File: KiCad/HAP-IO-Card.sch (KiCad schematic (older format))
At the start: 18 parts, among them U1 D1_Mini, U10 7400, U2 PCF8574, U3 PCF8574, U4 PCF8574, U5 PCF8574, U6 PCF8574, U7 PCF8574, U8 PCF8574, U9 PCF8574

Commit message: ESP32 component and footprint
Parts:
- removed R1, R2, R3, R4, R5, R6, R7, R8: 10k, Resistors_SMD:R_0603, symbol R
- removed U1: D1_Mini, D1-MINI, symbol D1_Mini
- removed U10: 7400, Housings_SSOP:TSSOP-14_4.4x5mm_Pitch0.65mm, symbol 7400
- removed U2, U3, U4, U5, U6, U7, U8, U9: PCF8574, Housings_SOIC:SOIC-16W_7.5x10.3mm_Pitch1.27mm, symbol PCF8574
- added SPRKESP321: Spark_ESP32Thing, spark_esp32thing:Sparkfun_ESP32Thing, symbol Spark_ESP32Thing-RESCUE-HAP-IO-Card
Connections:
- net labels removed: +5V, GND, VDD
- wire segments 75 -> 0
- no-connect marks 1 -> 0

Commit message: More work
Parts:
- removed SPRKESP321: Spark_ESP32Thing, spark_esp32thing:Sparkfun_ESP32Thing, symbol Spark_ESP32Thing-RESCUE-HAP-IO-Card
- added C1, C2, C3, C4, C5, C6, C7, C8: 10uF, Capacitors_SMD:C_0805, symbol CP
- added J1: DI1, Connectors_Terminal_Blocks:TerminalBlock_Pheonix_MPT-2.54mm_2pol, symbol Screw_Terminal_1x02
- added J2: DI2, Connectors_Terminal_Blocks:TerminalBlock_Pheonix_MPT-2.54mm_2pol, symbol Screw_Terminal_1x02
- added J3: DI3, Connectors_Terminal_Blocks:TerminalBlock_Pheonix_MPT-2.54mm_2pol, symbol Screw_Terminal_1x02
- added J4: DI4, Connectors_Terminal_Blocks:TerminalBlock_Pheonix_MPT-2.54mm_2pol, symbol Screw_Terminal_1x02
- added J5: DI5, Connectors_Terminal_Blocks:TerminalBlock_Pheonix_MPT-2.54mm_2pol, symbol Screw_Terminal_1x02
- added J6: DI6, Connectors_Terminal_Blocks:TerminalBlock_Pheonix_MPT-2.54mm_2pol, symbol Screw_Terminal_1x02
- added J7: DI7, Connectors_Terminal_Blocks:TerminalBlock_Pheonix_MPT-2.54mm_2pol, symbol Screw_Terminal_1x02
- added J8: DI8, Connectors_Terminal_Blocks:TerminalBlock_Pheonix_MPT-2.54mm_2pol, symbol Screw_Terminal_1x02
- added R1, R2, R3, R4, R5, R6, R7, R8: R, Resistors_SMD:R_0805, symbol R
- added R10, R11, R12, R13, R14, R15, R16, R9: 100, Resistors_SMD:R_0603, symbol R
- added RN1: 10k, Resistors_THT:R_Array_SIP9, symbol R_Network08
- added SPRKESP1: Spark_ESP32Thing, spark_esp32thing:Sparkfun_ESP32Thing, symbol Spark_ESP32Thing
- added U1, U2, U3, U4, U5, U6, U7, U8: LTV-354T, LTV-354T_MiniFlat:LTV-354T_MiniFlat, symbol LTV-354T
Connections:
- net labels added: +3.3V, DI1, DI2, DI3, DI4, DI5, DI6, DI7, DI8, GND
- wire segments 0 -> 80
- no-connect marks 0 -> 5
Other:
- note added: "Select based on input voltage.\nMax 50mA"

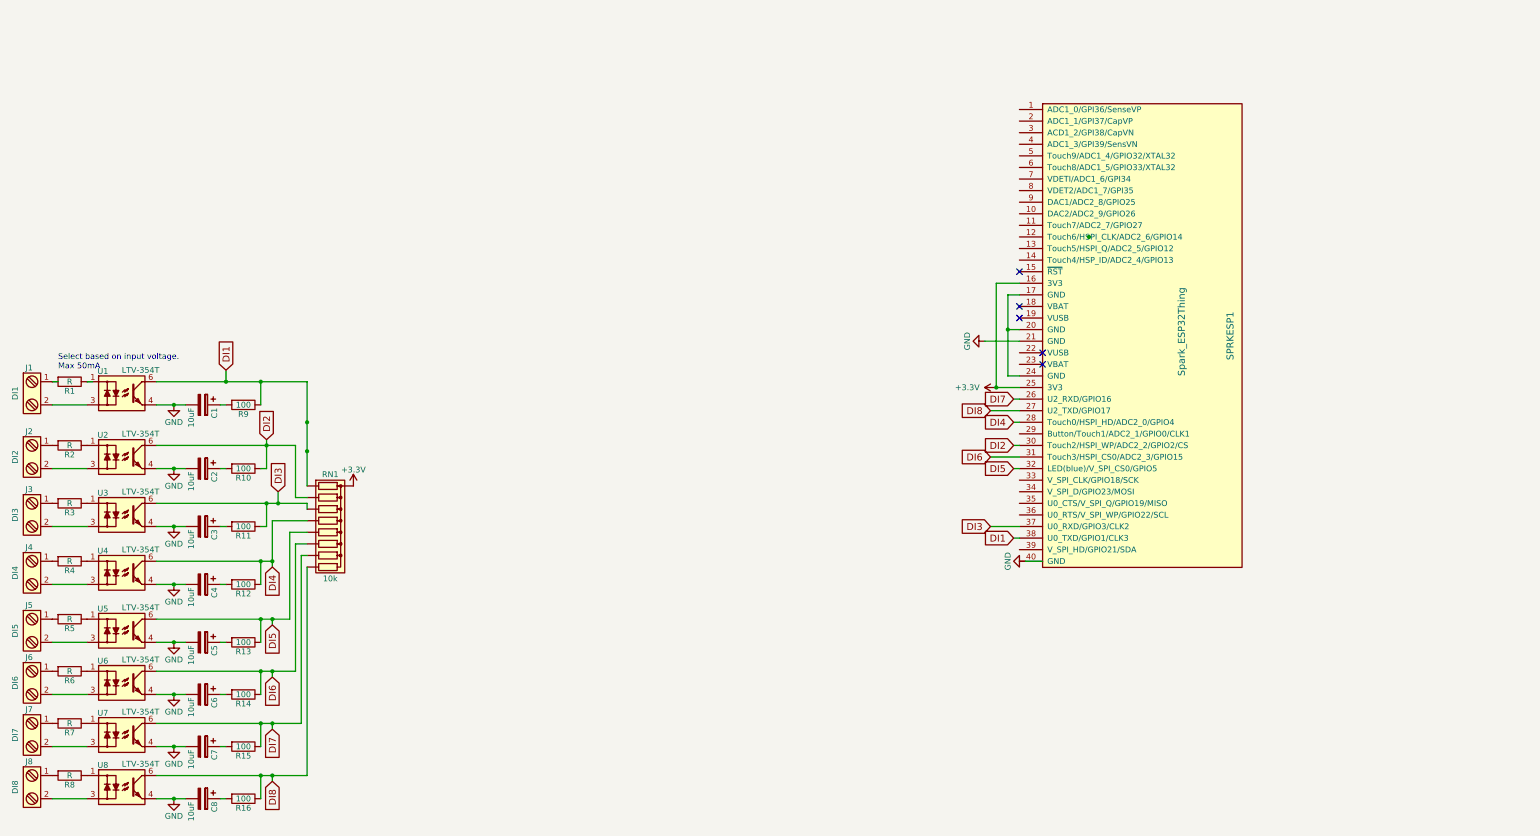
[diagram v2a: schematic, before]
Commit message: Split into separate schemas
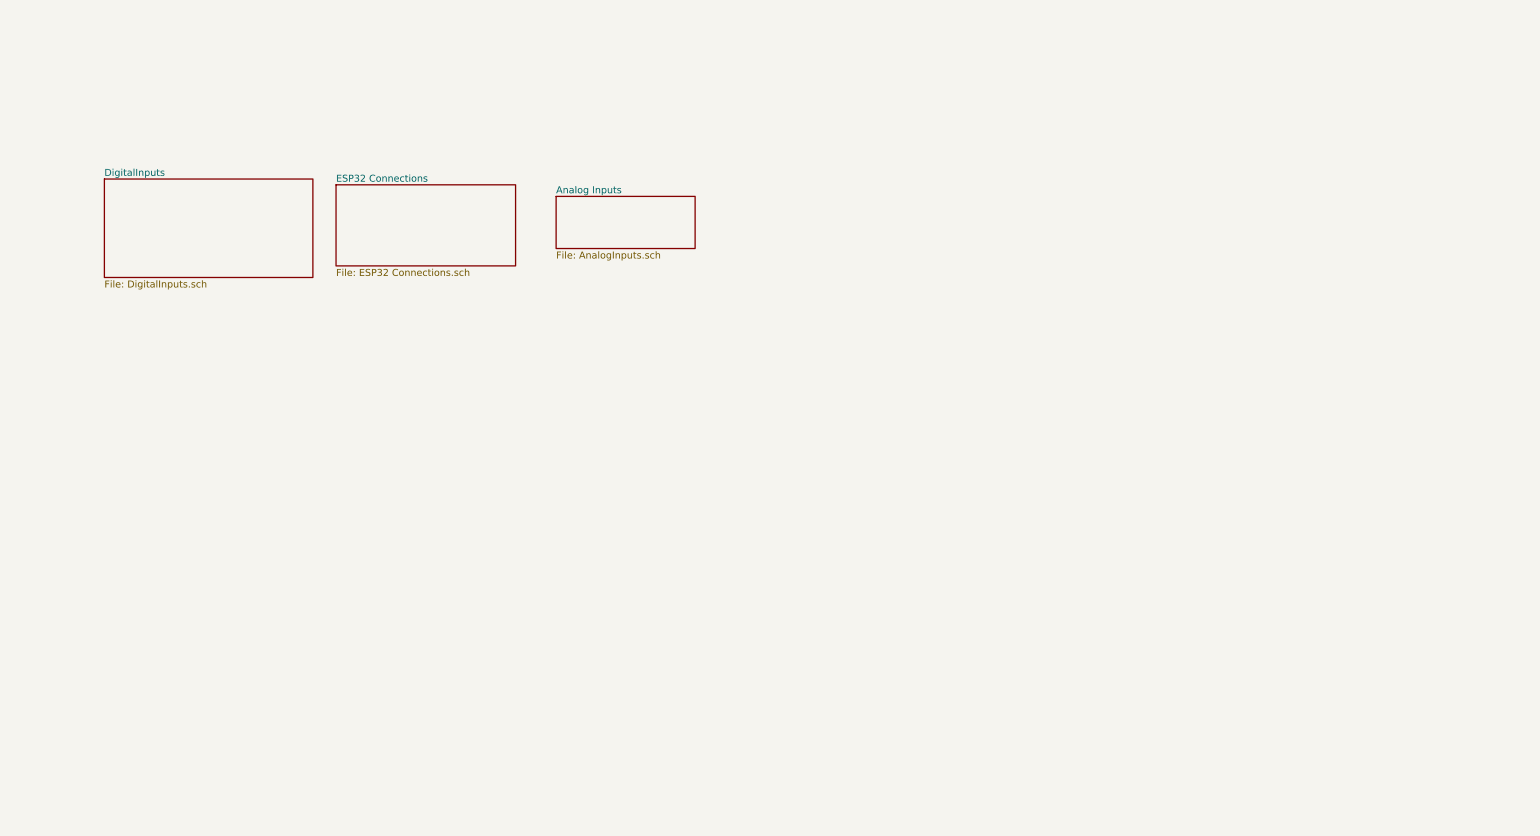
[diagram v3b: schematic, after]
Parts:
- removed C1, C2, C3, C4, C5, C6, C7, C8: 10uF, Capacitors_SMD:C_0805, symbol CP
- removed J1: DI1, Connectors_Terminal_Blocks:TerminalBlock_Pheonix_MPT-2.54mm_2pol, symbol Screw_Terminal_1x02
- removed J2: DI2, Connectors_Terminal_Blocks:TerminalBlock_Pheonix_MPT-2.54mm_2pol, symbol Screw_Terminal_1x02
- removed J3: DI3, Connectors_Terminal_Blocks:TerminalBlock_Pheonix_MPT-2.54mm_2pol, symbol Screw_Terminal_1x02
- removed J4: DI4, Connectors_Terminal_Blocks:TerminalBlock_Pheonix_MPT-2.54mm_2pol, symbol Screw_Terminal_1x02
- removed J5: DI5, Connectors_Terminal_Blocks:TerminalBlock_Pheonix_MPT-2.54mm_2pol, symbol Screw_Terminal_1x02
- removed J6: DI6, Connectors_Terminal_Blocks:TerminalBlock_Pheonix_MPT-2.54mm_2pol, symbol Screw_Terminal_1x02
- removed J7: DI7, Connectors_Terminal_Blocks:TerminalBlock_Pheonix_MPT-2.54mm_2pol, symbol Screw_Terminal_1x02
- removed J8: DI8, Connectors_Terminal_Blocks:TerminalBlock_Pheonix_MPT-2.54mm_2pol, symbol Screw_Terminal_1x02
- removed R1, R2, R3, R4, R5, R6, R7, R8: R, Resistors_SMD:R_0805, symbol R
- removed R10, R11, R12, R13, R14, R15, R16, R9: 100, Resistors_SMD:R_0603, symbol R
- removed RN1: 10k, Resistors_THT:R_Array_SIP9, symbol R_Network08
- removed SPRKESP1: Spark_ESP32Thing, spark_esp32thing:Sparkfun_ESP32Thing, symbol Spark_ESP32Thing
- removed U1, U2, U3, U4, U5, U6, U7, U8: LTV-354T, LTV-354T_MiniFlat:LTV-354T_MiniFlat, symbol LTV-354T
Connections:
- net labels removed: +3.3V, DI1, DI2, DI3, DI4, DI5, DI6, DI7, DI8, GND
- wire segments 80 -> 0
- no-connect marks 5 -> 0
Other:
- note removed: "Select based on input voltage.\nMax 50mA"

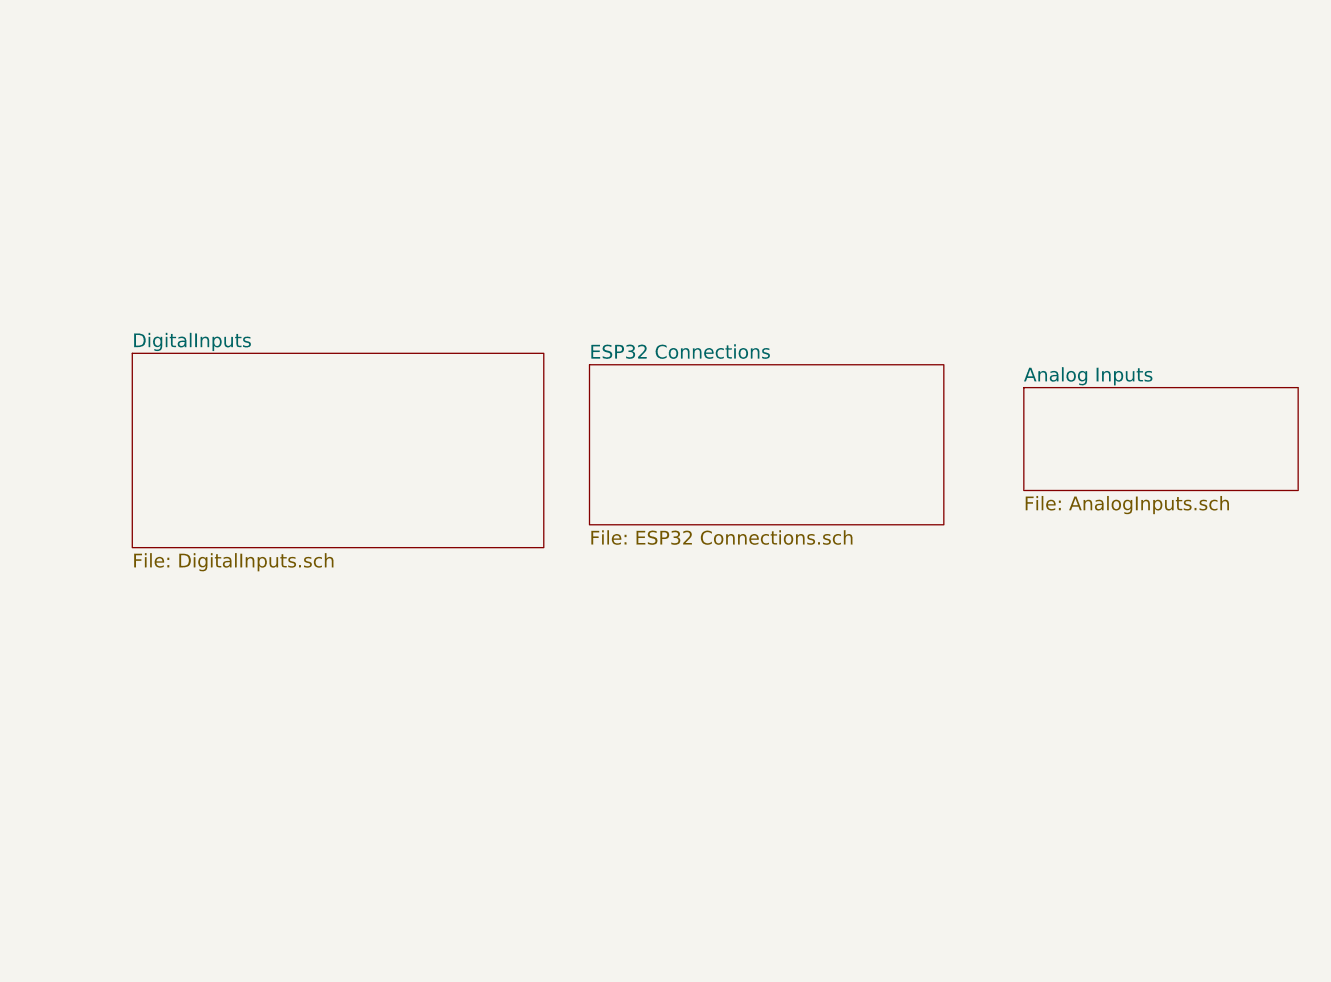
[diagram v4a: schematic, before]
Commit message: Added power supply
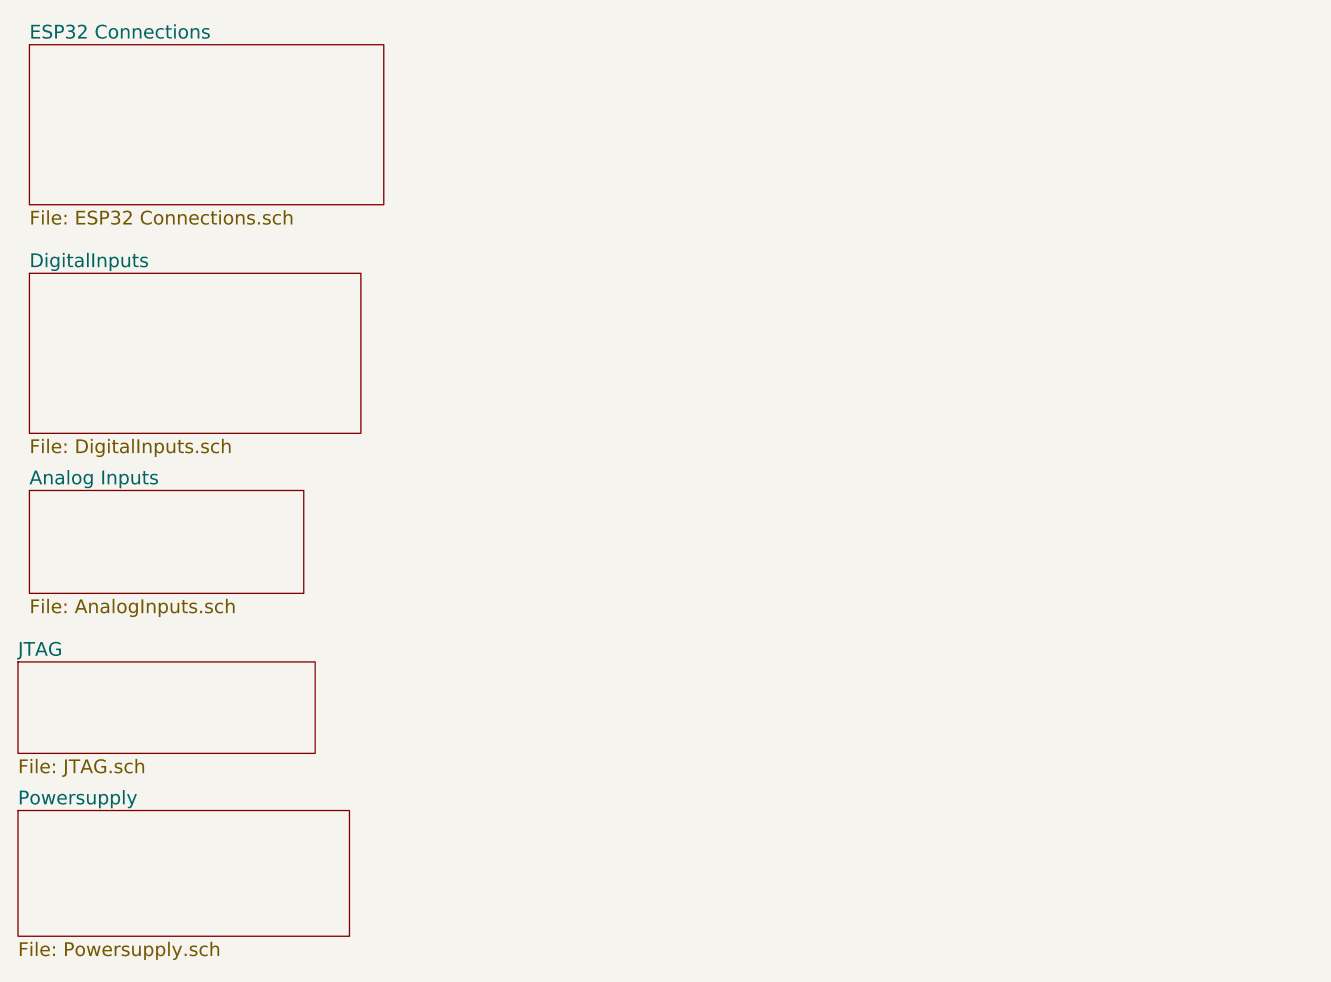
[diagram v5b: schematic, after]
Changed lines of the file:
@@
 LIBS:valves
 LIBS:spark_esp32thing
+LIBS:Power_Management
+LIBS:dc-dc
+LIBS:diode
+LIBS:ESD_Protection
+LIBS:SRR1260-330M
 LIBS:HAP-IO-Card-cache
 EELAYER 26 0
@@
 $Descr A4 11693 8268
 encoding utf-8
-Sheet 1 4
+Sheet 1 6
 Title ""
 Date ""
@@
 $EndDescr
 $Sheet
-S 1350 2150 1800 850
+S 900  1800 1450 700
 U 591810E7
 F0 "DigitalInputs" 60
@@
 $EndSheet
 $Sheet
-S 3350 2200 1550 700
+S 900  800  1550 700
 U 59181FE5
 F0 "ESP32 Connections" 60
@@
 $EndSheet
 $Sheet
-S 5250 2300 1200 450
+S 900  2750 1200 450
 U 591A7DC8
 F0 "Analog Inputs" 60
 F1 "AnalogInputs.sch" 60
 $EndSheet
+$Sheet
+S 850  4150 1450 550
+U 591CB050
+F0 "Powersupply" 60
+F1 "Powersupply.sch" 60
+$EndSheet
+$Sheet
+S 850  3500 1300 400
+U 591CB087
+F0 "JTAG" 60
+F1 "JTAG.sch" 60
+$EndSheet
 $EndSCHEMATC

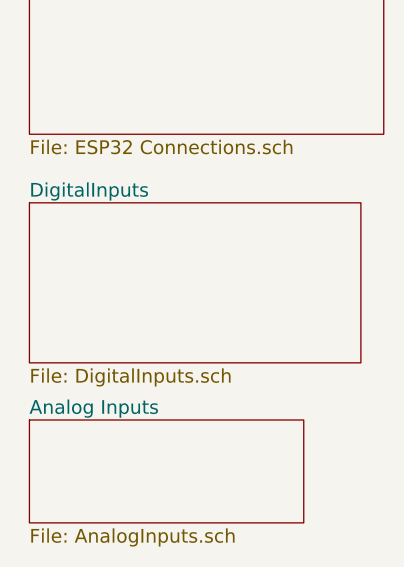
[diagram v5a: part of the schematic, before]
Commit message: Use I2C for I/O
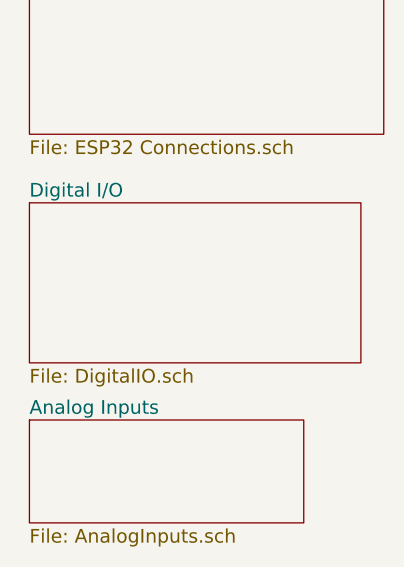
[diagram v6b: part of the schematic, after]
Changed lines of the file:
@@
 LIBS:ESD_Protection
 LIBS:SRR1260-330M
+LIBS:ADS1115IDGST
 LIBS:HAP-IO-Card-cache
 EELAYER 26 0
@@
 S 900  1800 1450 700
 U 591810E7
-F0 "DigitalInputs" 60
-F1 "DigitalInputs.sch" 60
+F0 "Digital I/O" 60
+F1 "DigitalIO.sch" 60
 $EndSheet
 $Sheet

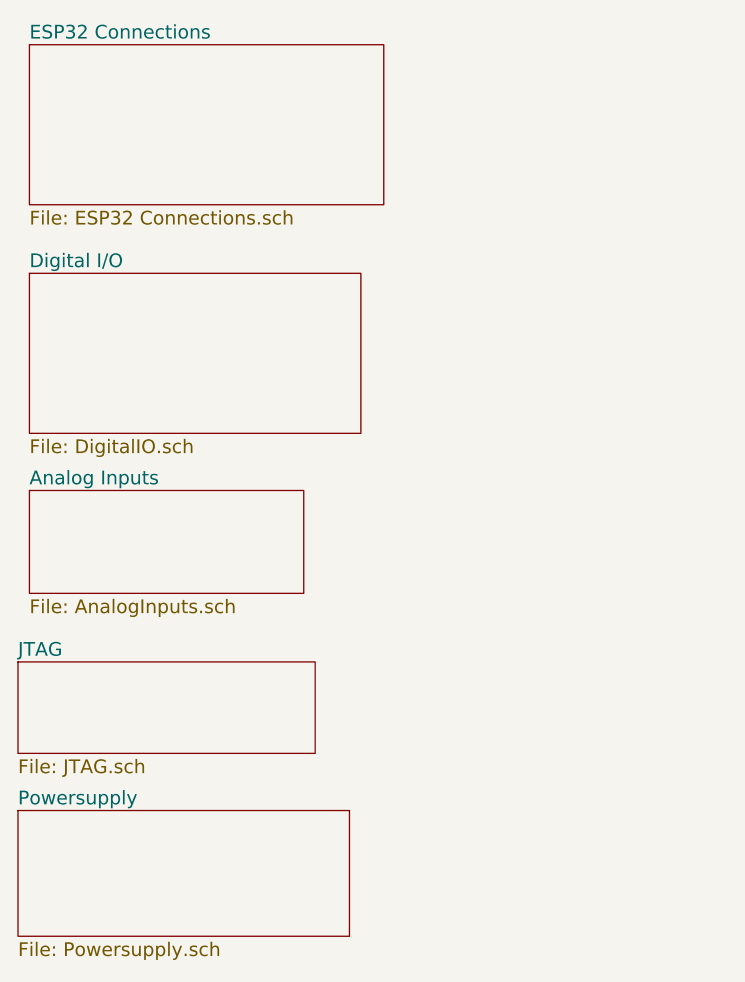
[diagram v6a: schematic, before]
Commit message: Reworked power-supply to provide 5V. Updated ESP-connections.
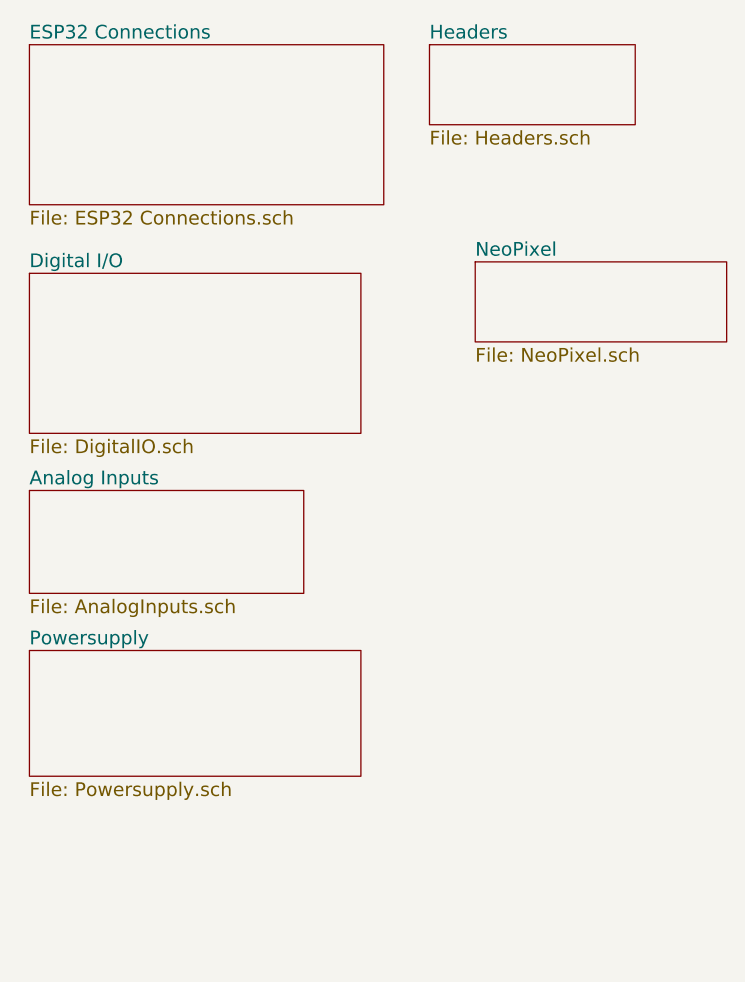
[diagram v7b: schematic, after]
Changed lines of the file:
@@
 LIBS:SRR1260-330M
 LIBS:ADS1115IDGST
+LIBS:LM1086
 LIBS:HAP-IO-Card-cache
 EELAYER 26 0
@@
 $Descr A4 11693 8268
 encoding utf-8
-Sheet 1 6
+Sheet 1 7
 Title ""
 Date ""
@@
 $EndSheet
 $Sheet
-S 850  4150 1450 550
+S 900  3450 1450 550
 U 591CB050
 F0 "Powersupply" 60
@@
 $EndSheet
 $Sheet
-S 850  3500 1300 400
-U 591CB087
-F0 "JTAG" 60
-F1 "JTAG.sch" 60
+S 2650 800  900  350
+U 5924A2C7
+F0 "Headers" 60
+F1 "Headers.sch" 60
+$EndSheet
+$Sheet
+S 2850 1750 1100 350
+U 5924F41E
+F0 "NeoPixel" 60
+F1 "NeoPixel.sch" 60
 $EndSheet
 $EndSCHEMATC

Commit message: More work
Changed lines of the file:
@@
 EESchema Schematic File Version 2
-LIBS:HAP-IO-Card-rescue
 LIBS:power
 LIBS:device
@@
 $EndSheet
 $Sheet
-S 2850 1750 1100 350
+S 2650 1800 1100 350
 U 5924F41E
 F0 "NeoPixel" 60
